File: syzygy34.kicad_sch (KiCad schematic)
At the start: 55 parts, among them J30 292161-3, J31 292161-3, J32 SYZYGY_SOCKET-STD, J33 SYZYGY_SOCKET-STD, U21 XC7Z030_FBG676

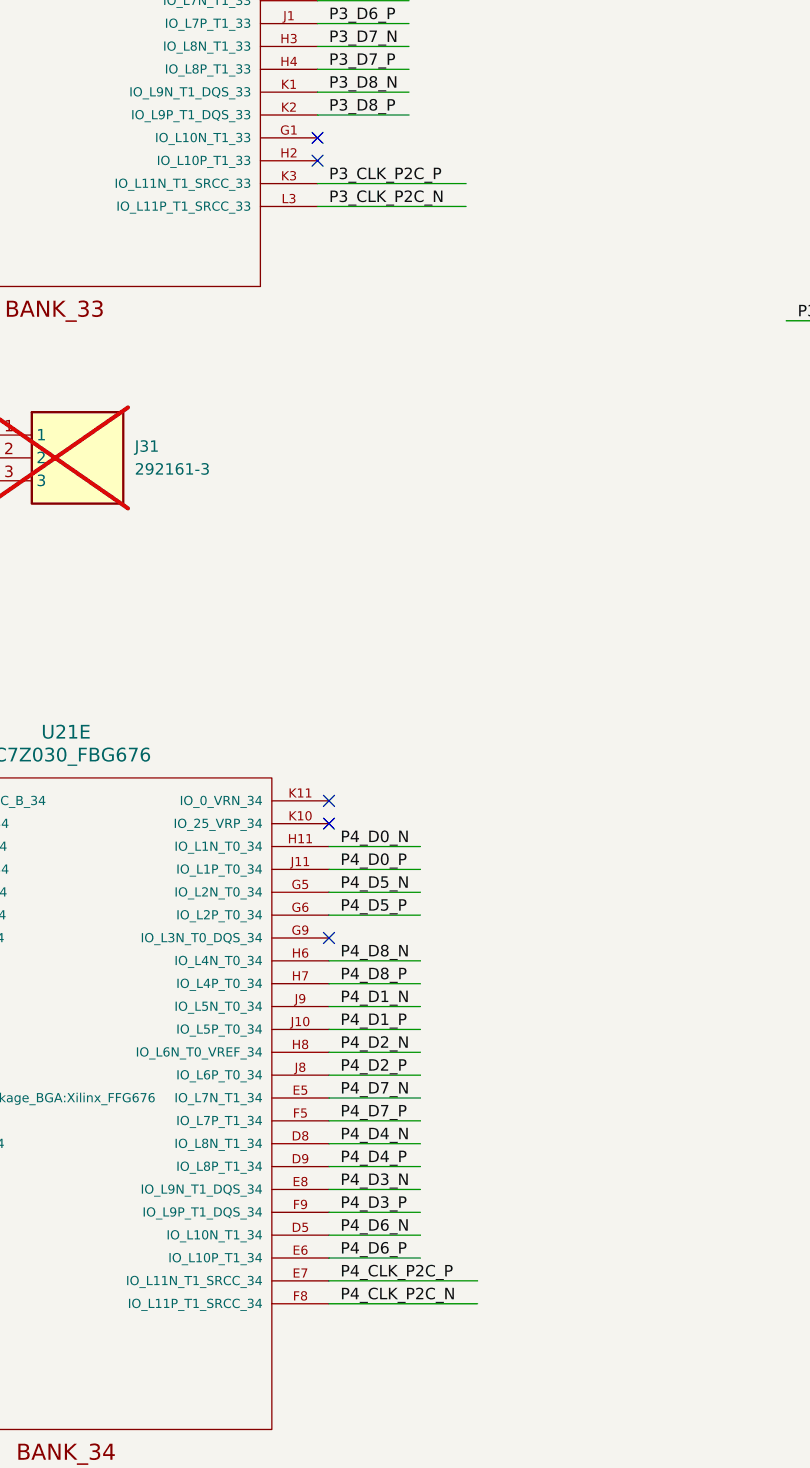
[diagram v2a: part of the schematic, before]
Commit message: P2C SYZYGY clock lines polarity fix, allow Y3 TCXO with pin1 ENA
Swapped polarity on SYZYGY P2C clock lines were fixed
Two additional resistors R71 & R64 were introduced to allow a TCXO with ENA input
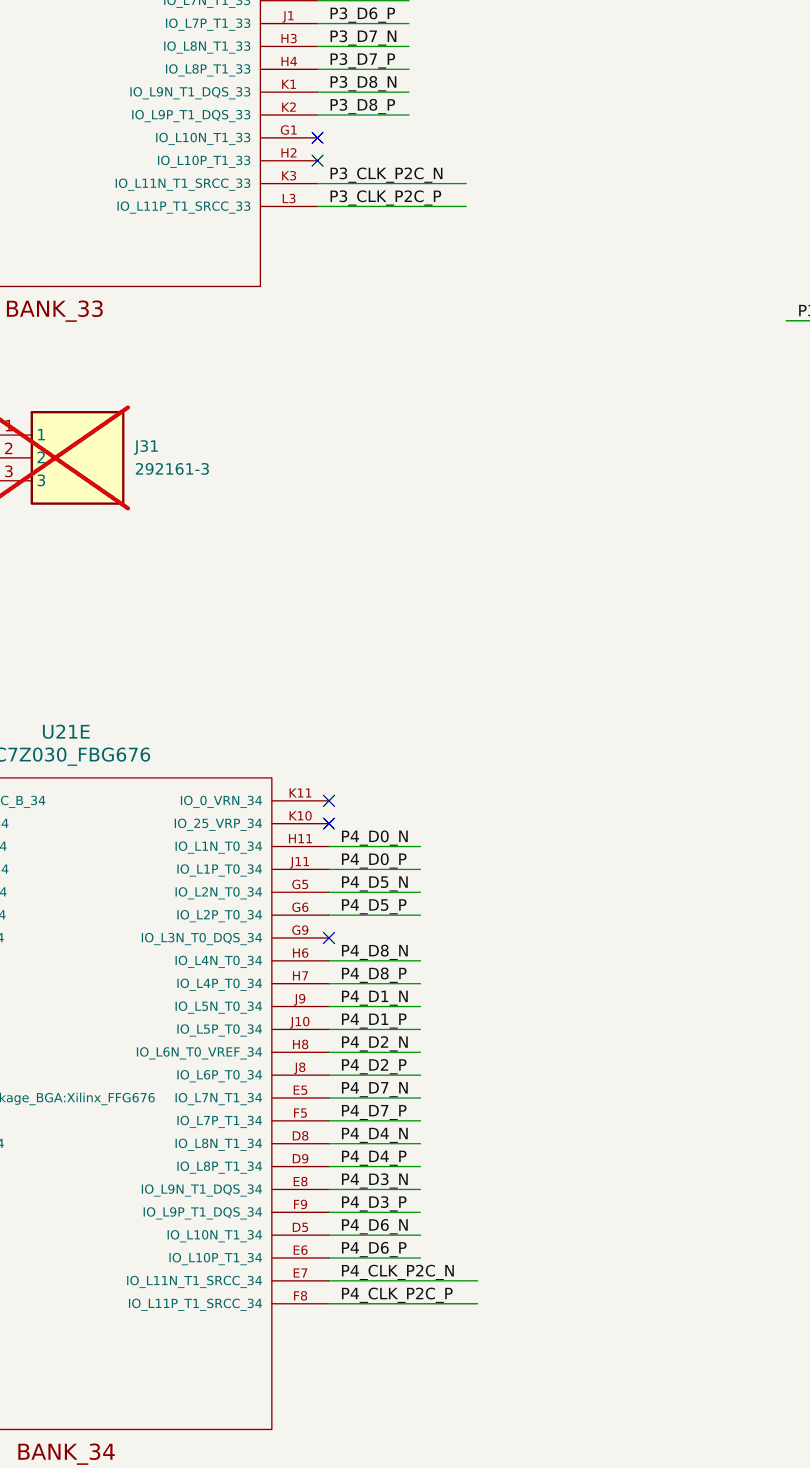
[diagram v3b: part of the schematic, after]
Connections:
- net P3_CLK_P2C_N: now also U21.K3 (IO_L11N_T1_SRCC_33); no longer U21.L3 (IO_L11P_T1_SRCC_33)
- net P3_CLK_P2C_P: now also U21.L3 (IO_L11P_T1_SRCC_33); no longer U21.K3 (IO_L11N_T1_SRCC_33)
- net P4_CLK_P2C_N: now also U21.E7 (IO_L11N_T1_SRCC_34); no longer U21.F8 (IO_L11P_T1_SRCC_34)
- net P4_CLK_P2C_P: now also U21.F8 (IO_L11P_T1_SRCC_34); no longer U21.E7 (IO_L11N_T1_SRCC_34)
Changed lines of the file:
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@@
-		)
-	)
-	(label "P3_CLK_P2C_P"
-		(at 134.62 93.98 0)
-		(effects
-			(font
-				(size 1.27 1.27)
-			)
-			(justify left bottom)
 		)
 	)
@@
 		)
 	)
-	(label "P4_CLK_P2C_N"
-		(at 135.89 218.44 0)
-		(effects
-			(font
-				(size 1.27 1.27)
-			)
-			(justify left bottom)
-		)
-	)
 	(label "P4_D6_P"
 		(at 135.89 213.36 0)
@@
 		)
 	)
+	(label "P3_CLK_P2C_N"
+		(at 134.62 93.98 0)
+		(effects
+			(font
+				(size 1.27 1.27)
+			)
+			(justify left bottom)
+		)
+	)
 	(label "P4_D3_P"
 		(at 332.74 179.07 0)
@@
 		)
 	)
-	(label "P3_CLK_P2C_N"
-		(at 134.62 96.52 0)
-		(effects
-			(font
-				(size 1.27 1.27)
-			)
-			(justify left bottom)
-		)
-	)
 	(label "I2C_PSSZG4.I2C_SCL"
 		(at 49.53 195.58 0)
@@
 		)
 	)
-	(label "P4_CLK_P2C_P"
-		(at 135.89 215.9 0)
-		(effects
-			(font
-				(size 1.27 1.27)
-			)
-			(justify left bottom)
-		)
-	)
 	(label "P4_D0_N"
 		(at 135.89 167.64 0)
@@
 		)
 	)
+	(label "P4_CLK_P2C_N"
+		(at 135.89 215.9 0)
+		(effects
+			(font
+				(size 1.27 1.27)
+			)
+			(justify left bottom)
+		)
+	)
 	(label "P3_C2P_P"
 		(at 320.04 83.82 0)
@@
 		)
 	)
+	(label "P3_CLK_P2C_P"
+		(at 134.62 96.52 0)
+		(effects
+			(font
+				(size 1.27 1.27)
+			)
+			(justify left bottom)
+		)
+	)
 	(label "P3_D1_N"
 		(at 134.62 48.26 0)
@@
 		(effects
 			(font
+				(size 1.27 1.27)
+			)
+			(justify left bottom)
+		)
+	)
+	(label "P4_CLK_P2C_P"
+		(at 135.89 218.44 0)
+		(effects
+			(font
